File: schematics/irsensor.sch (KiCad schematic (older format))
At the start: 11 parts, among them Q1 NPN, Q2 NPN

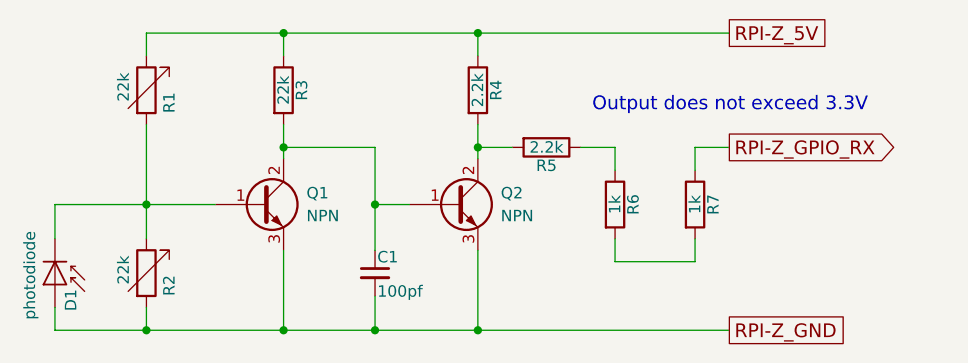
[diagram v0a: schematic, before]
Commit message: fix error in schematics
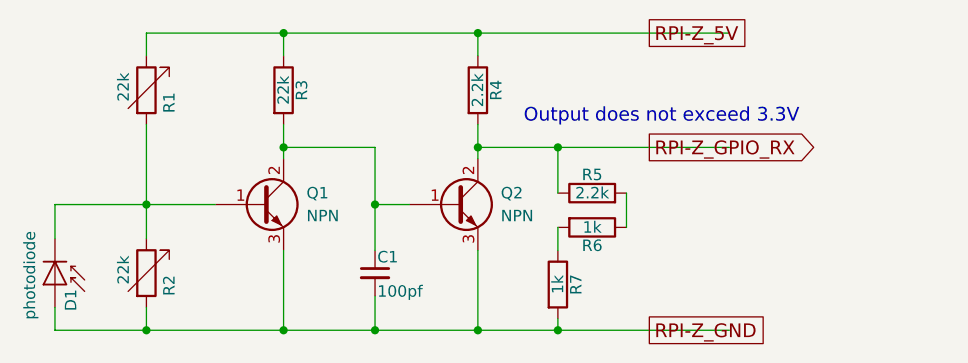
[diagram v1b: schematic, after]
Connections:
- wire segments 26 -> 36
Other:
- moved on the sheet: R5, R6, R7
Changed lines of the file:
@@
-EESchema Schematic File Version 2
-LIBS:power
-LIBS:device
-LIBS:switches
-LIBS:relays
-LIBS:motors
-LIBS:transistors
-LIBS:conn
-LIBS:linear
-LIBS:regul
-LIBS:74xx
-LIBS:cmos4000
-LIBS:adc-dac
-LIBS:memory
-LIBS:xilinx
-LIBS:microcontrollers
-LIBS:dsp
-LIBS:microchip
-LIBS:analog_switches
-LIBS:motorola
-LIBS:texas
-LIBS:intel
-LIBS:audio
-LIBS:interface
-LIBS:digital-audio
-LIBS:philips
-LIBS:display
-LIBS:cypress
-LIBS:siliconi
-LIBS:opto
-LIBS:atmel
-LIBS:contrib
-LIBS:valves
-EELAYER 25 0
+EESchema Schematic File Version 4
+EELAYER 30 0
 EELAYER END
 $Descr A4 11693 8268
@@
 L R R5
 U 1 1 5DDDA555
-P 5350 2350
-F 0 "R5" V 5430 2350 50  0000 C CNN
-F 1 "2.2k" V 5350 2350 50  0000 C CNN
-F 2 "" V 5280 2350 50  0001 C CNN
-F 3 "" H 5350 2350 50  0001 C CNN
-	1    5350 2350
-	0    1    1    0
-$EndComp
-$Comp
-L R R6
-U 1 1 5DDDA8B2
-P 5650 2600
-F 0 "R6" V 5730 2600 50  0000 C CNN
-F 1 "1k" V 5650 2600 50  0000 C CNN
-F 2 "" V 5580 2600 50  0001 C CNN
-F 3 "" H 5650 2600 50  0001 C CNN
-	1    5650 2600
-	1    0    0    -1
+P 5550 2550
+F 0 "R5" V 5630 2550 50  0000 C CNN
+F 1 "2.2k" V 5550 2550 50  0000 C CNN
+F 2 "" V 5480 2550 50  0001 C CNN
+F 3 "" H 5550 2550 50  0001 C CNN
+	1    5550 2550
+	0    -1   -1   0
 $EndComp
 $Comp
 L R R7
 U 1 1 5DDDACA1
-P 6000 2600
-F 0 "R7" V 6080 2600 50  0000 C CNN
-F 1 "1k" V 6000 2600 50  0000 C CNN
-F 2 "" V 5930 2600 50  0001 C CNN
-F 3 "" H 6000 2600 50  0001 C CNN
-	1    6000 2600
+P 5400 2950
+F 0 "R7" V 5480 2950 50  0000 C CNN
+F 1 "1k" V 5400 2950 50  0000 C CNN
+F 2 "" V 5330 2950 50  0001 C CNN
+F 3 "" H 5400 2950 50  0001 C CNN
+	1    5400 2950
 	1    0    0    -1
 $EndComp
@@
 $EndComp
 Wire Wire Line
-	3600 2250 3600 2750
-Wire Wire Line
-	5050 2250 5050 2400
-Wire Wire Line
-	4600 2350 4600 2800
+	3600 2250 3600 2600
+Wire Wire Line
+	5050 2250 5050 2350
+Wire Wire Line
+	4600 2350 4600 2600
 Connection ~ 4600 2600
 Wire Wire Line
-	4200 2250 4200 2400
+	4200 2250 4200 2350
 Wire Wire Line
 	4600 2600 4750 2600
@@
 Connection ~ 4200 2350
 Wire Wire Line
-	3200 3150 6150 3150
+	3200 3150 3600 3150
 Wire Wire Line
 	4200 3150 4200 2800
@@
 Connection ~ 4600 3150
 Wire Wire Line
-	3200 2600 3900 2600
+	3200 2600 3600 2600
 Connection ~ 3600 2600
 Wire Wire Line
-	3600 1850 6150 1850
+	3600 1850 4200 1850
 Wire Wire Line
 	4200 1850 4200 1950
@@
 Wire Wire Line
 	3200 2600 3200 2750
-Wire Wire Line
-	5200 2350 5050 2350
 Connection ~ 5050 2350
-Wire Wire Line
-	5500 2350 5650 2350
-Wire Wire Line
-	5650 2350 5650 2450
-Wire Wire Line
-	5650 2750 5650 2850
-Wire Wire Line
-	5650 2850 6000 2850
-Wire Wire Line
-	6000 2850 6000 2750
-Wire Wire Line
-	6000 2450 6000 2350
-Text GLabel 6150 2350 2    60   Output ~ 0
+Text GLabel 5800 2350 2    60   Output ~ 0
 RPI-Z_GPIO_RX
-Wire Wire Line
-	6000 2350 6150 2350
-Text GLabel 6150 3150 2    60   UnSpc ~ 0
+Text GLabel 5800 3150 2    60   UnSpc ~ 0
 RPI-Z_GND
-Text GLabel 6150 1850 2    60   UnSpc ~ 0
+Text GLabel 5800 1850 2    60   UnSpc ~ 0
 RPI-Z_5V
 Wire Wire Line
@@
 Connection ~ 5050 3150
 Connection ~ 5050 1850
-Text Notes 5550 2200 0    60   ~ 0
+Text Notes 5250 2250 0    60   ~ 0
 Output does not exceed 3.3V
+Wire Wire Line
+	4600 2600 4600 2800
+Wire Wire Line
+	4200 2350 4200 2400
+Wire Wire Line
+	4600 3150 5050 3150
+Wire Wire Line
+	3600 2600 3600 2750
+Wire Wire Line
+	3600 2600 3900 2600
+Wire Wire Line
+	4200 1850 5050 1850
+Wire Wire Line
+	5050 2350 5050 2400
+Wire Wire Line
+	4200 3150 4600 3150
+Wire Wire Line
+	3600 3150 4200 3150
+Wire Wire Line
+	5050 1850 6150 1850
+$Comp
+L R R6
+U 1 1 5DDDA8B2
+P 5550 2700
+F 0 "R6" V 5630 2700 50  0000 C CNN
+F 1 "1k" V 5550 2700 50  0000 C CNN
+F 2 "" V 5480 2700 50  0001 C CNN
+F 3 "" H 5550 2700 50  0001 C CNN
+	1    5550 2700
+	0    1    1    0
+$EndComp
+Wire Wire Line
+	5050 2350 5400 2350
+Wire Wire Line
+	5050 3150 5400 3150
+Wire Wire Line
+	5400 2550 5400 2350
+Connection ~ 5400 2350
+Wire Wire Line
+	5400 2350 6150 2350
+Wire Wire Line
+	5700 2550 5700 2700
+Wire Wire Line
+	5400 2700 5400 2800
+Wire Wire Line
+	5400 3100 5400 3150
+Connection ~ 5400 3150
+Wire Wire Line
+	5400 3150 6150 3150
 $EndSCHEMATC
